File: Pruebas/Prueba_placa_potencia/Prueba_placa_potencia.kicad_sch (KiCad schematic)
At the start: 54 parts, among them J1 Conn_01x03_Pin, J2 Conn_01x03_Pin, J3 Screw_Terminal_01x02, J4 Screw_Terminal_01x02, J6 Conn_01x03_Pin, J7 LOAD+, J8 LOAD-, Q1 2N2222A, Q10 2N2222A, Q11 TIP142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

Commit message: Routing complete
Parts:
- C2, C3: footprint Capacitor_THT:CP_Radial_D5.0mm_P2.00mm -> Capacitor_THT:CP_Radial_D5.0mm_P2.50mm
- Q1, Q10, Q2, Q4, Q6, Q8: footprint Package_TO_SOT_THT:TO-92_Inline -> Package_TO_SOT_THT:TO-92L_Inline_Wide
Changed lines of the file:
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@@
 			)
 		)
-		(property "Footprint" "Package_TO_SOT_THT:TO-92_Inline"
+		(property "Footprint" "Package_TO_SOT_THT:TO-92L_Inline_Wide"
 			(at 109.22 86.36 0)
 			(effects
@@
 			)
 		)
-		(property "Footprint" "Package_TO_SOT_THT:TO-92_Inline"
+		(property "Footprint" "Package_TO_SOT_THT:TO-92L_Inline_Wide"
 			(at 162.56 66.04 0)
 			(effects
@@
 			)
 		)
-		(property "Footprint" "Package_TO_SOT_THT:TO-92_Inline"
+		(property "Footprint" "Package_TO_SOT_THT:TO-92L_Inline_Wide"
 			(at 146.05 66.04 0)
 			(effects
@@
 			)
 		)
-		(property "Footprint" "Package_TO_SOT_THT:TO-92_Inline"
+		(property "Footprint" "Package_TO_SOT_THT:TO-92L_Inline_Wide"
 			(at 180.34 66.04 0)
 			(effects
@@
 			)
 		)
-		(property "Footprint" "Capacitor_THT:CP_Radial_D5.0mm_P2.00mm"
+		(property "Footprint" "Capacitor_THT:CP_Radial_D5.0mm_P2.50mm"
 			(at 68.2752 97.79 0)
 			(effects
@@
 			)
 		)
-		(property "Footprint" "Package_TO_SOT_THT:TO-92_Inline"
+		(property "Footprint" "Package_TO_SOT_THT:TO-92L_Inline_Wide"
 			(at 129.54 66.04 0)
 			(effects
@@
 			)
 		)
-		(property "Footprint" "Capacitor_THT:CP_Radial_D5.0mm_P2.00mm"
+		(property "Footprint" "Capacitor_THT:CP_Radial_D5.0mm_P2.50mm"
 			(at 54.3052 97.79 0)
 			(effects
@@
 			)
 		)
-		(property "Footprint" "Package_TO_SOT_THT:TO-92_Inline"
+		(property "Footprint" "Package_TO_SOT_THT:TO-92L_Inline_Wide"
 			(at 114.3 66.04 0)
 			(effects

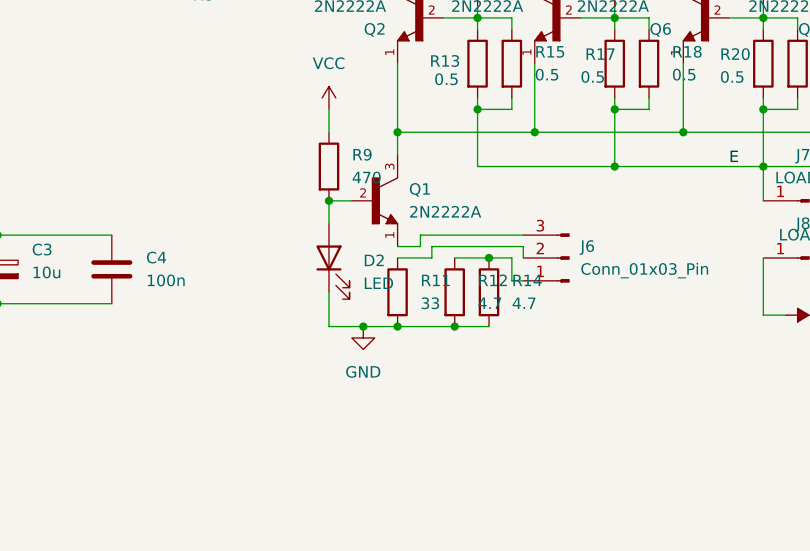
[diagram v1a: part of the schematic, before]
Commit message: Correct jumper connections
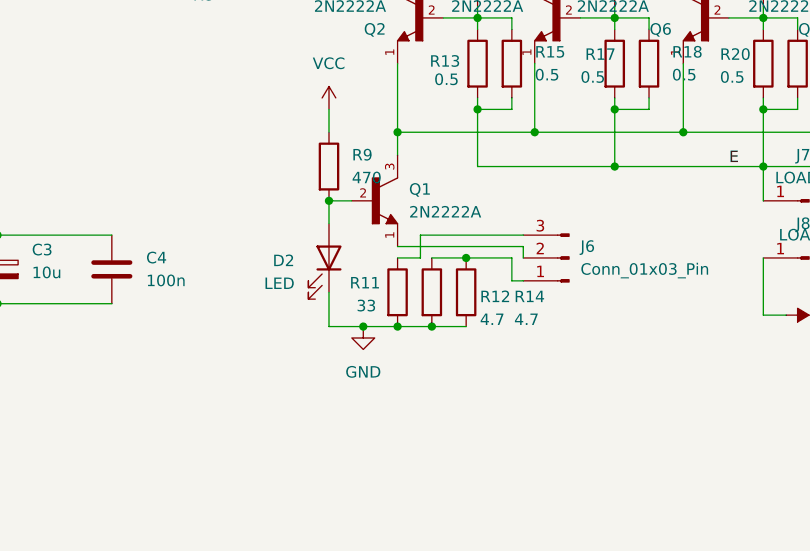
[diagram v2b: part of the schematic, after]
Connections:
- net at Q1.1: now also J6.2 (Pin_2); no longer J6.3 (Pin_3)
- net at R11.1: now also J6.3 (Pin_3); no longer J6.2 (Pin_2)
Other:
- moved on the sheet: D2, R12, R14
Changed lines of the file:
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@@
 	)
 	(junction
-		(at 118.11 100.33)
-		(diameter 0)
-		(color 0 0 0 0)
-	)
-	(junction
 		(at 168.91 66.04)
 		(diameter 0)
@@
 	)
 	(junction
+		(at 115.57 100.33)
+		(diameter 0)
+		(color 0 0 0 0)
+	)
+	(junction
 		(at 104.14 86.36)
 		(diameter 0)
@@
 	)
 	(junction
-		(at 67.31 90.17)
+		(at 119.38 92.71)
 		(diameter 0)
 		(color 0 0 0 0)
 	)
 	(junction
-		(at 50.8 44.45)
+		(at 67.31 90.17)
 		(diameter 0)
 		(color 0 0 0 0)
 	)
 	(junction
-		(at 40.64 54.61)
+		(at 50.8 44.45)
 		(diameter 0)
 		(color 0 0 0 0)
 	)
 	(junction
-		(at 111.76 100.33)
+		(at 40.64 54.61)
 		(diameter 0)
 		(color 0 0 0 0)
 	)
 	(junction
-		(at 121.92 92.71)
+		(at 111.76 100.33)
 		(diameter 0)
 		(color 0 0 0 0)
@@
 	(wire
 		(pts
-			(xy 63.5 57.15) (xy 63.5 49.53)
+			(xy 111.76 92.71) (xy 114.3 92.71)
 		)
 		(stroke
@@
 	(wire
 		(pts
-			(xy 30.48 50.8) (xy 30.48 54.61)
+			(xy 63.5 57.15) (xy 63.5 49.53)
 		)
 		(stroke
@@
 	(wire
 		(pts
-			(xy 139.7 74.93) (xy 139.7 76.2)
+			(xy 30.48 50.8) (xy 30.48 54.61)
 		)
 		(stroke
@@
 	(wire
 		(pts
-			(xy 177.8 59.69) (xy 179.07 59.69)
+			(xy 139.7 74.93) (xy 139.7 76.2)
 		)
 		(stroke
@@
 	(wire
 		(pts
-			(xy 50.8 62.23) (xy 55.88 62.23)
+			(xy 177.8 59.69) (xy 179.07 59.69)
 		)
 		(stroke
@@
 	(wire
 		(pts
-			(xy 172.72 76.2) (xy 168.91 76.2)
+			(xy 50.8 62.23) (xy 55.88 62.23)
 		)
 		(stroke
@@
 	(wire
 		(pts
-			(xy 40.64 44.45) (xy 44.45 44.45)
+			(xy 172.72 76.2) (xy 168.91 76.2)
 		)
 		(stroke
@@
 	(wire
 		(pts
-			(xy 168.91 76.2) (xy 168.91 74.93)
+			(xy 40.64 44.45) (xy 44.45 44.45)
 		)
 		(stroke
@@
 	(wire
 		(pts
-			(xy 115.57 92.71) (xy 115.57 91.44)
+			(xy 168.91 76.2) (xy 168.91 74.93)
 		)
 		(stroke
@@
 	(wire
 		(pts
-			(xy 118.11 100.33) (xy 121.92 100.33)
-		)
-		(stroke
-			(width 0)
-			(type default)
-		)
-	)
-	(wire
-		(pts
 			(xy 83.82 46.99) (xy 83.82 48.26)
 		)
@@
 	(wire
 		(pts
-			(xy 121.92 92.71) (xy 124.46 92.71)
-		)
-		(stroke
-			(width 0)
-			(type default)
-		)
-	)
-	(wire
-		(pts
 			(xy 104.14 96.52) (xy 104.14 100.33)
 		)
@@
 	(wire
 		(pts
-			(xy 111.76 100.33) (xy 118.11 100.33)
+			(xy 111.76 100.33) (xy 115.57 100.33)
 		)
 		(stroke
@@
 	(wire
 		(pts
-			(xy 83.82 46.99) (xy 80.01 46.99)
+			(xy 115.57 100.33) (xy 119.38 100.33)
 		)
 		(stroke
@@
 	(wire
 		(pts
-			(xy 127 40.64) (xy 127 46.99)
+			(xy 83.82 46.99) (xy 80.01 46.99)
 		)
 		(stroke
@@
 	(wire
 		(pts
-			(xy 17.78 43.18) (xy 17.78 46.99)
+			(xy 127 40.64) (xy 127 46.99)
 		)
 		(stroke
@@
 	(wire
 		(pts
-			(xy 127 46.99) (xy 135.89 46.99)
+			(xy 17.78 43.18) (xy 17.78 46.99)
 		)
 		(stroke
@@
 	(wire
 		(pts
-			(xy 83.82 55.88) (xy 83.82 57.15)
+			(xy 127 46.99) (xy 135.89 46.99)
 		)
 		(stroke
@@
 	(wire
 		(pts
-			(xy 114.3 91.44) (xy 114.3 90.17)
+			(xy 83.82 55.88) (xy 83.82 57.15)
 		)
 		(stroke
@@
 	(wire
 		(pts
-			(xy 127 59.69) (xy 127 60.96)
+			(xy 114.3 90.17) (xy 125.73 90.17)
 		)
 		(stroke
@@
 	(wire
 		(pts
-			(xy 168.91 66.04) (xy 168.91 67.31)
+			(xy 127 59.69) (xy 127 60.96)
 		)
 		(stroke
@@
 	(wire
 		(pts
-			(xy 114.3 90.17) (xy 125.73 90.17)
+			(xy 168.91 66.04) (xy 168.91 67.31)
 		)
 		(stroke
@@
 	(wire
 		(pts
-			(xy 125.73 91.44) (xy 125.73 92.71)
-		)
-		(stroke
-			(width 0)
-			(type default)
-		)
-	)
-	(wire
-		(pts
 			(xy 93.98 57.15) (xy 99.06 57.15)
 		)
@@
 	(wire
 		(pts
-			(xy 115.57 91.44) (xy 125.73 91.44)
-		)
-		(stroke
-			(width 0)
-			(type default)
-		)
-	)
-	(wire
-		(pts
-			(xy 118.11 92.71) (xy 121.92 92.71)
+			(xy 115.57 92.71) (xy 119.38 92.71)
 		)
 		(stroke
@@
 	(wire
 		(pts
-			(xy 46.99 90.17) (xy 46.99 92.71)
+			(xy 114.3 92.71) (xy 114.3 90.17)
 		)
 		(stroke
@@
 	(wire
 		(pts
-			(xy 63.5 49.53) (xy 64.77 49.53)
+			(xy 46.99 90.17) (xy 46.99 92.71)
 		)
 		(stroke
@@
 	(wire
 		(pts
-			(xy 40.64 46.99) (xy 40.64 50.8)
+			(xy 63.5 49.53) (xy 64.77 49.53)
 		)
 		(stroke
@@
 	(wire
 		(pts
-			(xy 156.21 74.93) (xy 156.21 76.2)
+			(xy 40.64 46.99) (xy 40.64 50.8)
 		)
 		(stroke
@@
 	(wire
 		(pts
-			(xy 111.76 92.71) (xy 115.57 92.71)
+			(xy 156.21 74.93) (xy 156.21 76.2)
 		)
 		(stroke
@@
 	(wire
 		(pts
+			(xy 111.76 91.44) (xy 125.73 91.44)
+		)
+		(stroke
+			(width 0)
+			(type default)
+		)
+	)
+	(wire
+		(pts
 			(xy 40.64 46.99) (xy 40.64 44.45)
 		)
@@
 	(wire
 		(pts
-			(xy 168.91 82.55) (xy 186.69 82.55)
+			(xy 119.38 92.71) (xy 124.46 92.71)
 		)
 		(stroke
@@
 	(wire
 		(pts
-			(xy 107.95 100.33) (xy 111.76 100.33)
+			(xy 125.73 91.44) (xy 125.73 92.71)
 		)
 		(stroke
@@
 	(wire
 		(pts
-			(xy 111.76 91.44) (xy 114.3 91.44)
+			(xy 168.91 82.55) (xy 186.69 82.55)
+		)
+		(stroke
+			(width 0)
+			(type default)
+		)
+	)
+	(wire
+		(pts
+			(xy 107.95 100.33) (xy 111.76 100.33)
 		)
 		(stroke
@@
 	(symbol
 		(lib_id "Device:R")
-		(at 118.11 96.52 0)
+		(at 115.57 96.52 0)
 		(unit 1)
 		(exclude_from_sim no)
@@
 		(on_board yes)
 		(dnp no)
-		(fields_autoplaced yes)
 		(property "Reference" "R12"
-			(at 120.65 95.2499 0)
+			(at 120.904 97.028 0)
 			(effects
 				(font
@@
 		)
 		(property "Value" "4.7"
-			(at 120.65 97.7899 0)
+			(at 120.904 99.568 0)
 			(effects
 				(font
@@
 		)
 		(property "Footprint" "Resistor_THT:R_Axial_DIN0207_L6.3mm_D2.5mm_P7.62mm_Horizontal"
-			(at 116.332 96.52 90)
+			(at 113.792 96.52 90)
 			(effects
 				(font
@@
 		)
 		(property "Datasheet" "~"
-			(at 118.11 96.52 0)
+			(at 115.57 96.52 0)
 			(effects
 				(font
@@
 		)
 		(property "Description" "Resistor"
-			(at 118.11 96.52 0)
+			(at 115.57 96.52 0)
 			(effects
 				(font
@@
 	(symbol
 		(lib_id "Device:LED")
-		(at 104.14 92.71 90)
+		(at 104.14 92.71 270)
+		(mirror x)
 		(unit 1)
 		(exclude_from_sim no)
@@
 		(on_board yes)
 		(dnp no)
-		(fields_autoplaced yes)
 		(property "Reference" "D2"
-			(at 107.95 93.0274 90)
+			(at 100.33 93.0274 90)
 			(effects
 				(font
@@
 		)
 		(property "Value" "LED"
-			(at 107.95 95.5674 90)
+			(at 100.33 95.5674 90)
 			(effects
 				(font
@@
 	(symbol
 		(lib_id "Device:R")
-		(at 121.92 96.52 0)
+		(at 119.38 96.52 0)
 		(unit 1)
 		(exclude_from_sim no)
@@
 		(on_board yes)
 		(dnp no)
-		(fields_autoplaced yes)
 		(property "Reference" "R14"
-			(at 124.46 95.2499 0)
+			(at 124.714 97.028 0)
 			(effects
 				(font
@@
 		)
 		(property "Value" "4.7"
-			(at 124.46 97.7899 0)
+			(at 124.714 99.568 0)
 			(effects
 				(font
@@
 		)
 		(property "Footprint" "Resistor_THT:R_Axial_DIN0207_L6.3mm_D2.5mm_P7.62mm_Horizontal"
-			(at 120.142 96.52 90)
+			(at 117.602 96.52 90)
 			(effects
 				(font
@@
 		)
 		(property "Datasheet" "~"
-			(at 121.92 96.52 0)
+			(at 119.38 96.52 0)
 			(effects
 				(font
@@
 		)
 		(property "Description" "Resistor"
-			(at 121.92 96.52 0)
+			(at 119.38 96.52 0)
 			(effects
 				(font
@@
 		(on_board yes)
 		(dnp no)
-		(fields_autoplaced yes)
 		(property "Reference" "R11"
-			(at 114.3 95.2499 0)
+			(at 106.426 95.504 0)
 			(effects
 				(font
@@
 		)
 		(property "Value" "33"
-			(at 114.3 97.7899 0)
+			(at 107.188 98.044 0)
 			(effects
 				(font
